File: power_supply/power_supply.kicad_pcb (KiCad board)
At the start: 2 copper layers, 150 x 70 mm, 55 parts, among them J1 Conn_01x04_Male, J2 Conn_01x03_Male, J3 Conn_01x03_Male, J4 Conn_01x03_Male, J5 Conn_01x02_Male, J6 Conn_01x02_Male, U1 LM7815_TO220, U2 LM7915_TO220, U3 LM7815_TO220

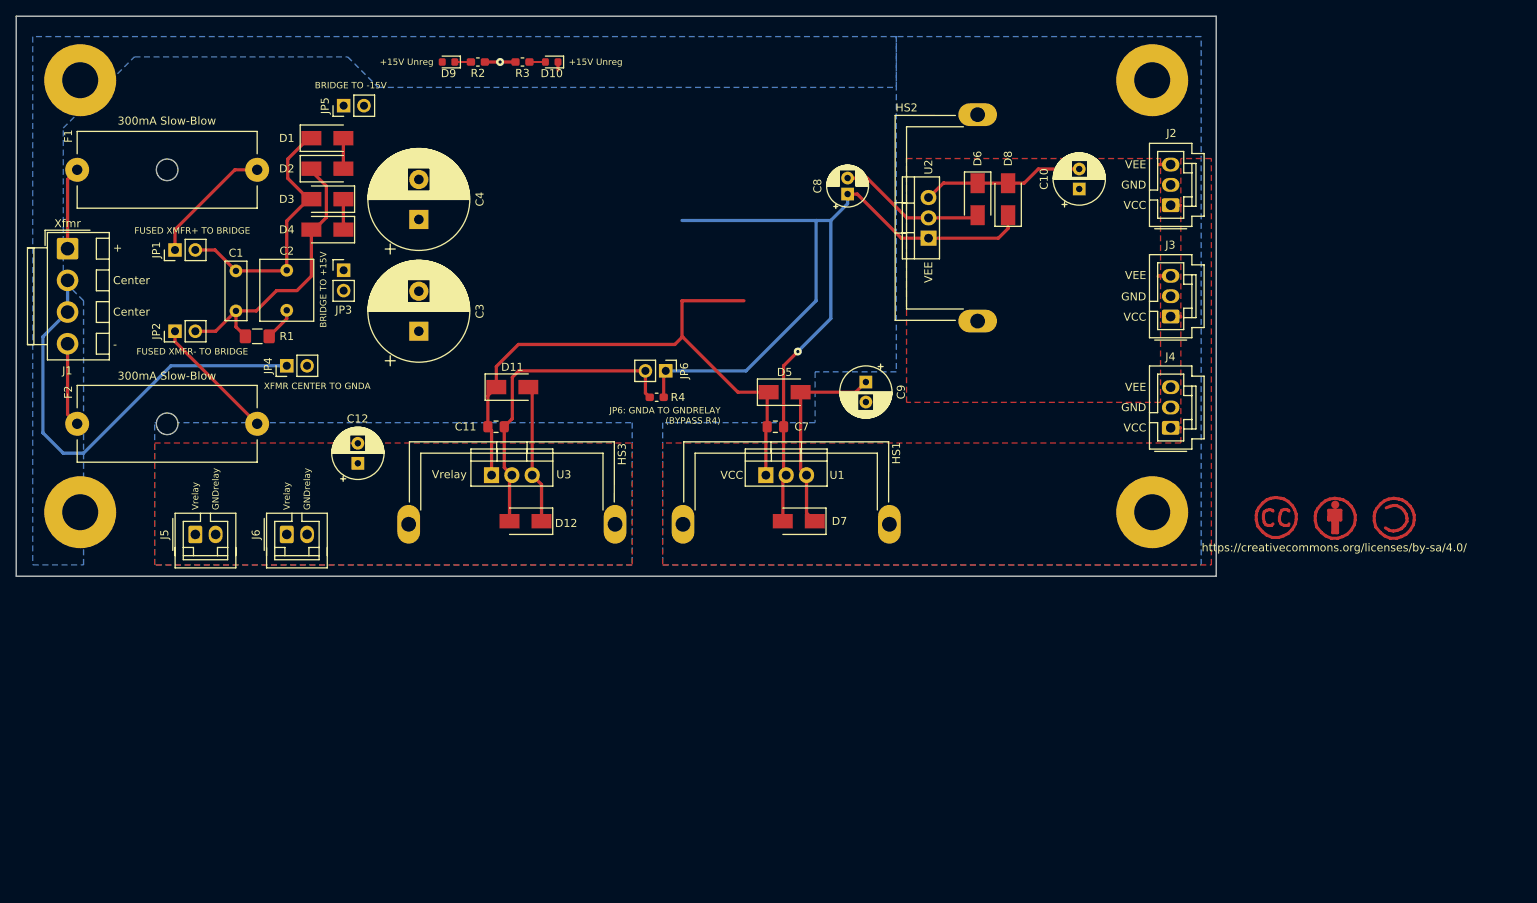
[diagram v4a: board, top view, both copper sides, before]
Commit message: correct silkscreen text for jumper JP6 based on schematic reannotation
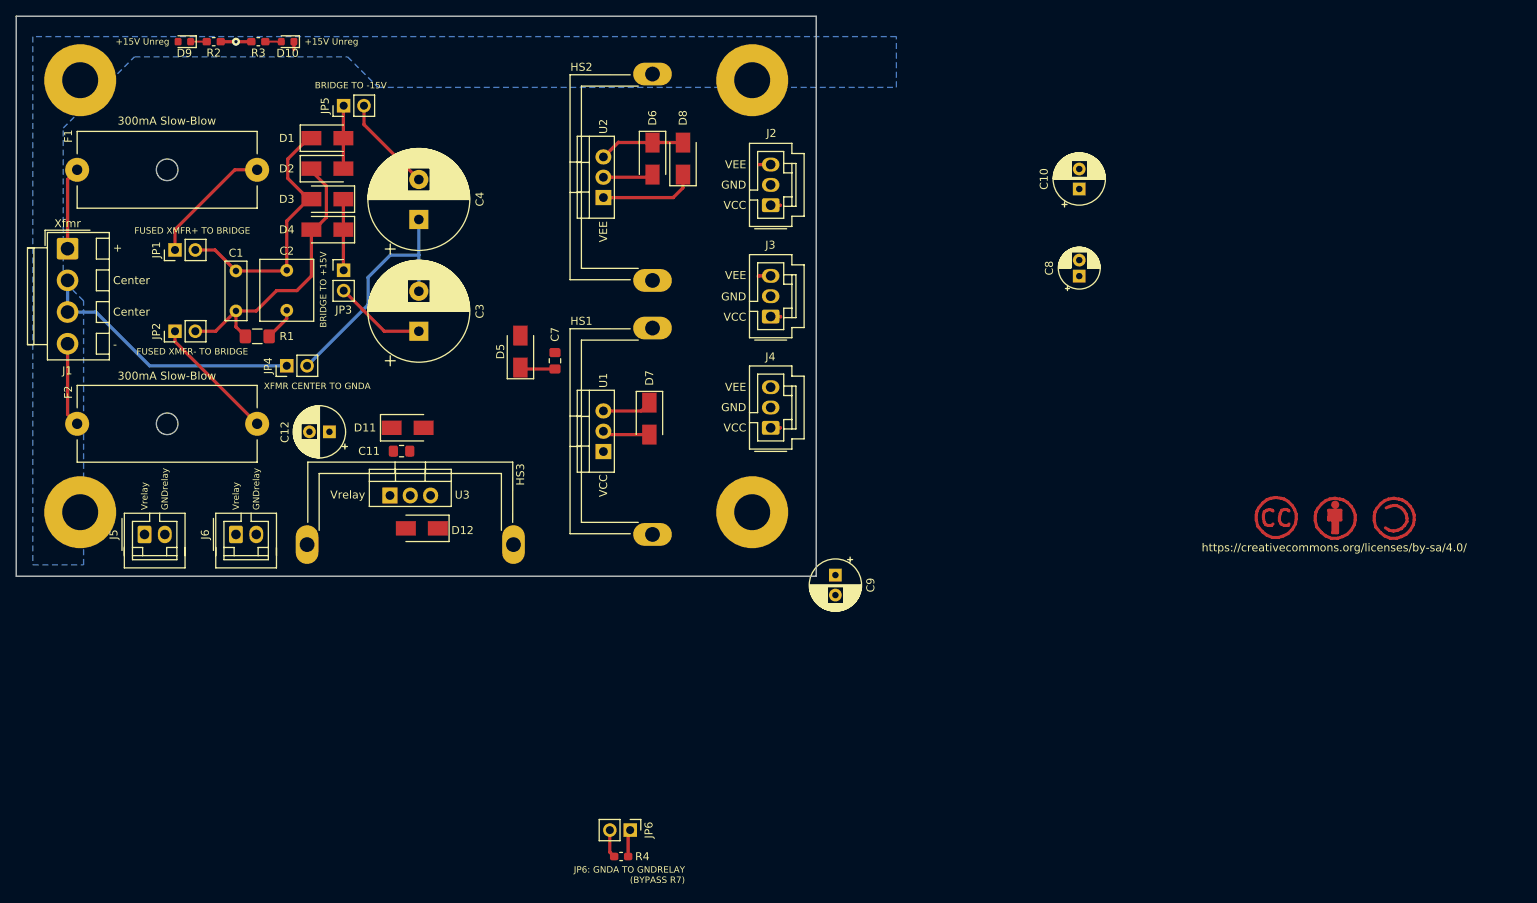
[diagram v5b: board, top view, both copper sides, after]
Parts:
- moved JP6 57.6 mm to (126.7, 181.7)
- moved R4 57.6 mm to (125.6, 185.0)
- moved H2 50.0 mm to (142.0, 88.0)
- moved H3 50.0 mm to (142.0, 142.0)
- moved J2 50.0 mm to (144.3, 103.6)
- moved J3 50.0 mm to (144.3, 117.5)
- moved J4 50.0 mm to (144.3, 131.5)
- moved D6 41.0 mm to (129.5, 97.8)
- moved D8 41.0 mm to (133.3, 97.8)
- moved HS2 41.0 mm to (129.5, 113.0)
- moved U2 41.0 mm to (123.4, 102.7)
- moved D5 33.4 mm to (113.0, 121.9), turned to 90 degrees
- moved D10 33.1 mm to (83.9, 83.2)
- moved R3 33.1 mm to (80.3, 83.2)
- moved D9 33.1 mm to (71.0, 83.2)
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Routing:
- net GNDA: track 128.5 -> 56.5 mm, vias 2 -> 1
- net /+15_unreg: track 75.8 -> 16.2 mm
- net GNDRELAY: track 39.4 -> 3.52 mm
- net /transformer_center: track 56.4 -> 34.1 mm
- net VCC: track 29.3 -> 9.90 mm
- net Vrelay: track 17.4 -> 0.00 mm
- net VEE: track 23.5 -> 13.8 mm
- net Net-(D3-Pad1): track 3.81 -> 8.90 mm
- net Net-(D1-Pad2): track 3.81 -> 7.89 mm
- removed copper zone on B.Cu, net GNDRELAY
- removed copper zone on F.Cu, net VCC
- removed copper zone on F.Cu, net VEE
- removed copper zone on F.Cu, net Vrelay
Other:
- board size 150 x 70 mm -> 100 x 70 mm
- board text added: "TODO fix C9, C10 add planes make smaller check to-220 dimensions for actual 7815 used add project rev, etc labels"
- board text removed: "TODO fix C9, C10 add planes make smaller check to-220 dimensions for actual 7815 used"

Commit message: finish basic routing. still need to thicken input traces, check TO-220 dims, and place labels/silkscreen decorations
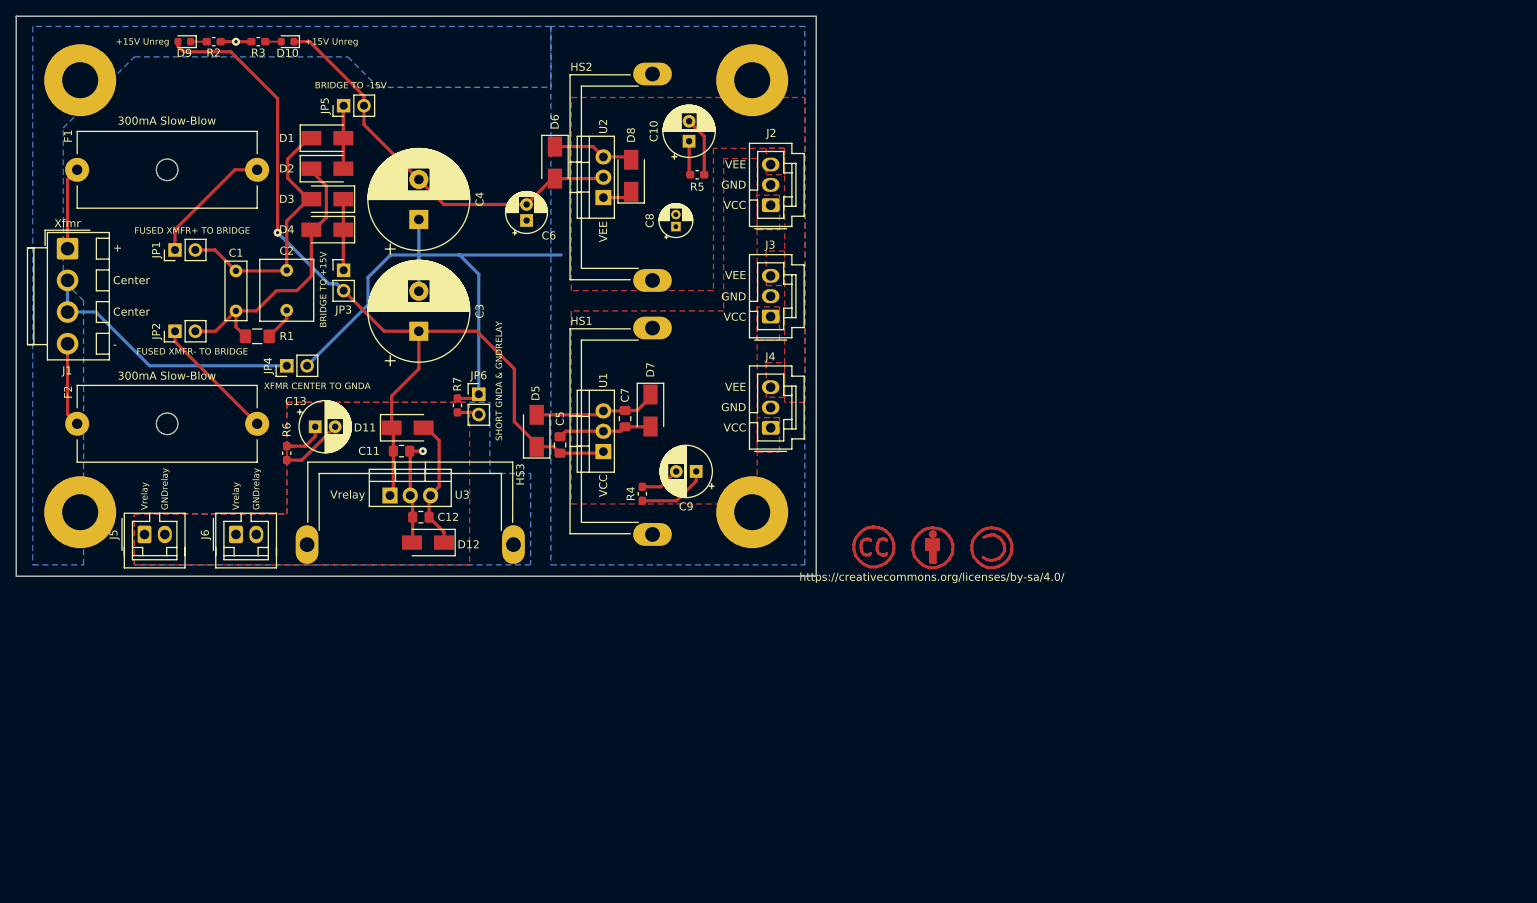
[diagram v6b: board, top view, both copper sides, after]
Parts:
- added C12: 100n, Capacitor_SMD:C_0805_2012Metric_Pad1.15x1.40mm_HandSolder, F.Cu at (100.6, 142.6)
- added C7: 100n, Capacitor_SMD:C_0805_2012Metric_Pad1.15x1.40mm_HandSolder, F.Cu at (126.1, 130.3)
- added C8: 1u, Capacitor_THT:CP_Radial_D4.0mm_P1.50mm, F.Cu at (132.5, 106.3)
- added R4: 100k, Capacitor_SMD:C_0603_1608Metric_Pad1.05x0.95mm_HandSolder, F.Cu at (128.3, 139.7)
- added R5: 100k, Capacitor_SMD:C_0603_1608Metric_Pad1.05x0.95mm_HandSolder, F.Cu at (135.1, 99.8)
- added R6: 100k, Capacitor_SMD:C_0603_1608Metric_Pad1.05x0.95mm_HandSolder, F.Cu at (83.8, 134.6)
- moved C6 69.4 mm to (113.8, 105.5)
- moved R7 60.0 mm to (105.2, 128.7), turned to 90 degrees
- moved JP6 57.7 mm to (107.8, 127.3), turned to 0 degrees
- moved REF** 50.4 mm to (157.1, 146.4)
- moved REF** 50.4 mm to (172.0, 146.4)
- moved REF** 50.4 mm to (164.6, 146.4)
- moved C10 49.1 mm to (134.1, 95.6)
- moved REF** 49.0 mm to (167.0, 119.9)
- moved REF** 47.5 mm to (175.0, 131.6)
- moved C9 21.7 mm to (135.0, 136.9), turned to 180 degrees
- moved D6 12.2 mm to (117.3, 98.3)
- moved C5 10.5 mm to (118.0, 133.6)
- moved D5 10.1 mm to (115.1, 131.8)
- moved D8 6.83 mm to (126.9, 99.9)
- moved D12 1.93 mm to (101.5, 145.8)
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- renumbered C12 to C13, C7 to C5, C8 to C6, R4 to R7
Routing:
- net /+15_unreg: track 16.2 -> 111.0 mm, vias 0 -> 1
- net GNDA: track 56.5 -> 99.0 mm
- net /-15_unreg: track 19.4 -> 50.7 mm
- net Vrelay: track 0.00 -> 21.9 mm
- net GNDRELAY: track 3.52 -> 23.8 mm, vias 0 -> 1
- net VCC: track 9.90 -> 24.4 mm
- net VEE: track 13.8 -> 17.7 mm
- added copper zone on B.Cu, net GNDRELAY
- added copper zone on F.Cu, net VCC
- added copper zone on F.Cu, net VEE
- added copper zone on F.Cu, net Vrelay
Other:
- net class grounds: clearance 0.4 -> 0.2
- board text added: "TODO add planes check to-220 dimensions for actual 7815 used add project rev, etc labels"
- board text removed: "TODO fix C9, C10 add planes make smaller check to-220 dimensions for actual 7815 used add project rev, etc labels"

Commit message: complete routing, including planes, thickening traces, and silkscreen labels
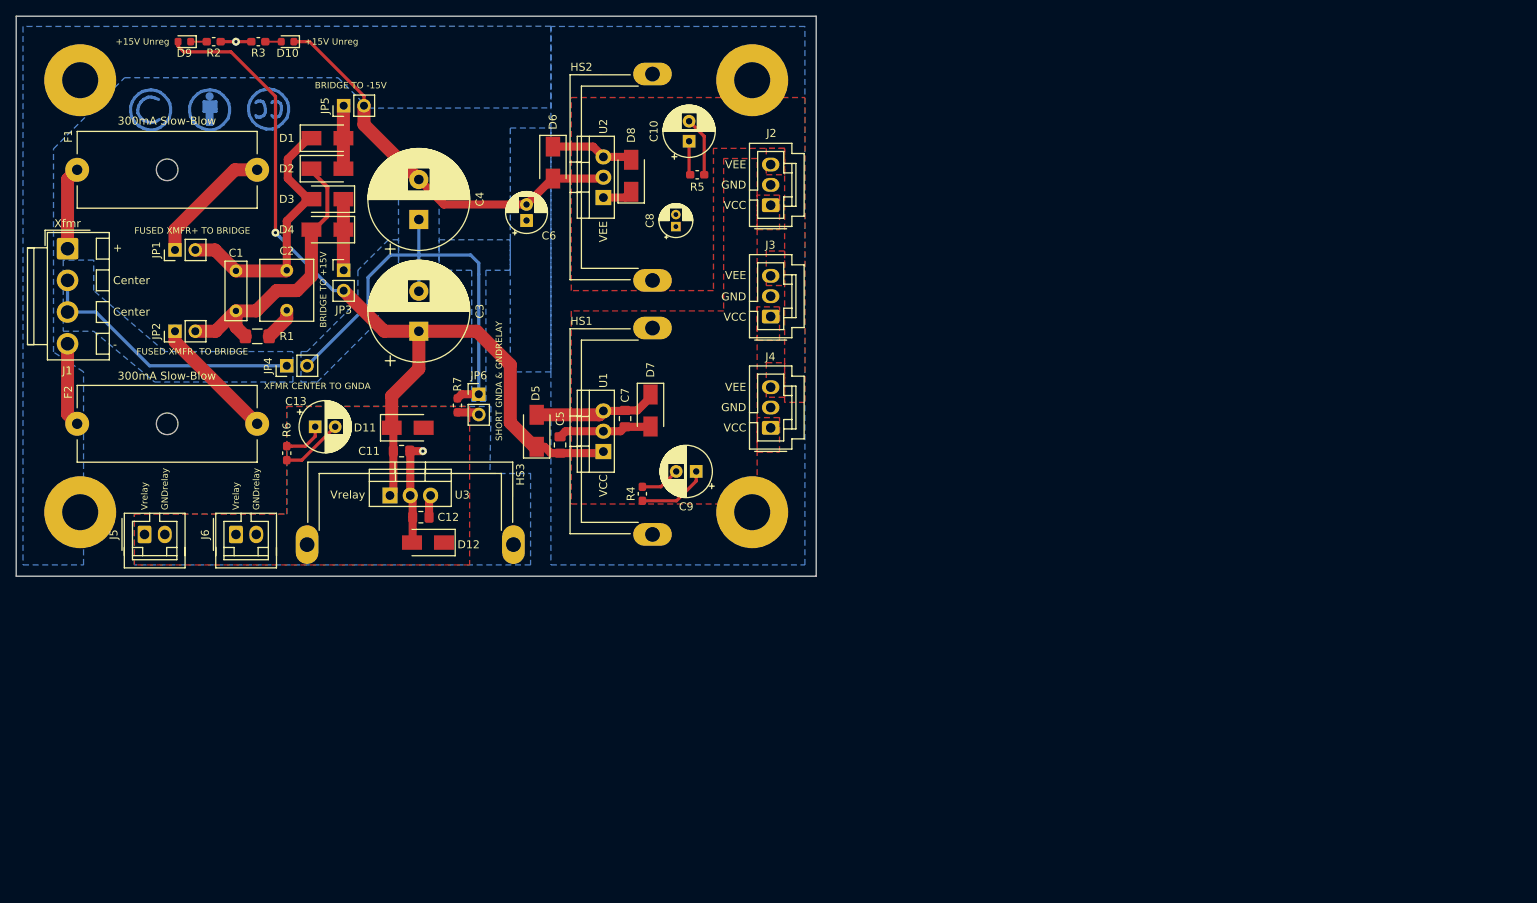
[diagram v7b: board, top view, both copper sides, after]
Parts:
- REF** (x3): moved to B.Cu
- moved REF** 118.5 mm to (66.8, 91.7), turned to 180 degrees
- moved REF** 105.7 mm to (74.2, 91.7), turned to 180 degrees
- moved REF** 93.1 mm to (81.7, 91.7), turned to 180 degrees
- moved REF** 73.4 mm to (110.5, 96.5)
- moved REF** 68.8 mm to (107.3, 85.6)
- moved D6 0.25 mm to (117.1, 98.3)
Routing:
- net Vrelay: track 21.9 -> 8.06 mm
- net GNDA: track 99.0 -> 87.1 mm
- added copper zone on B.Cu, net /transformer_center
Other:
- board text added: "Power Supply for Preamp 2019 rev0 G. Keeth"
- board text added: "TODO check to-220 dimensions for actual 7815 used"
- board text removed: "TODO add planes check to-220 dimensions for actual 7815 used add project rev, etc labels"

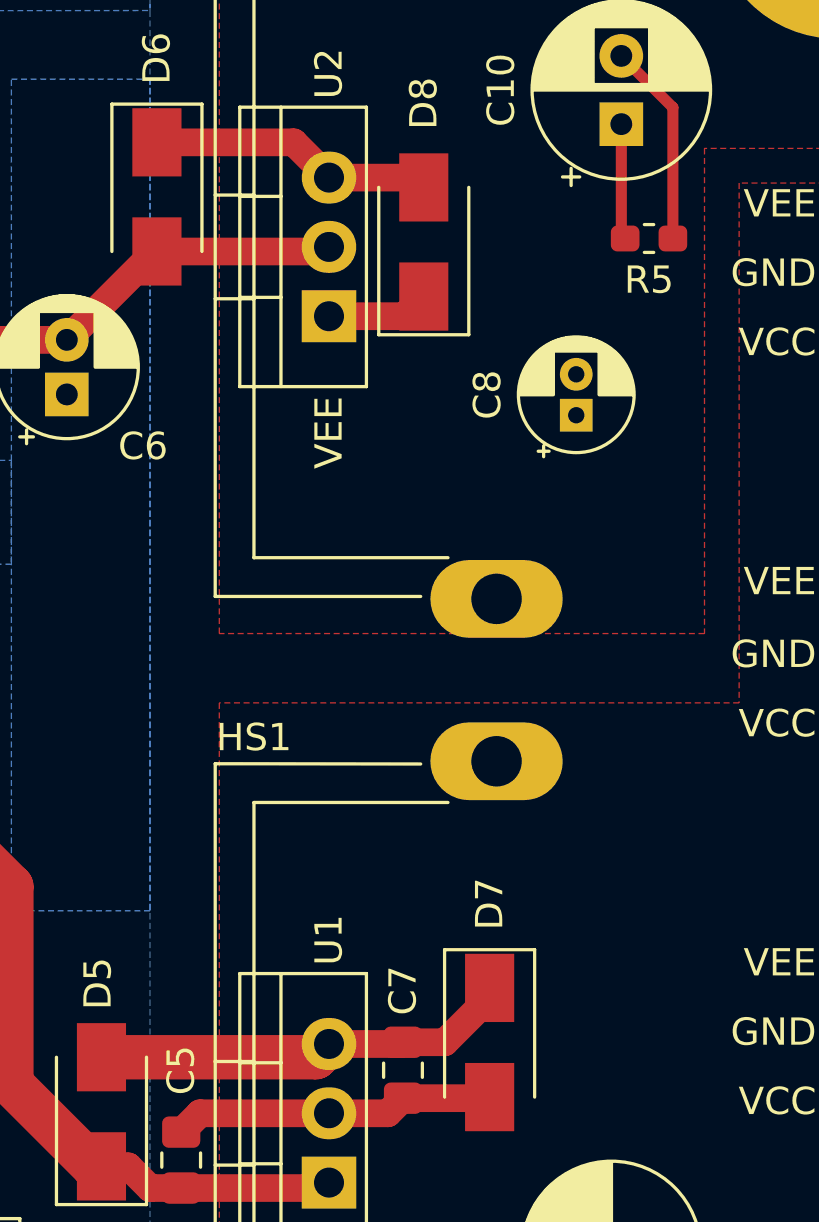
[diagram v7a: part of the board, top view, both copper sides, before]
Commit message: remove redundant traces
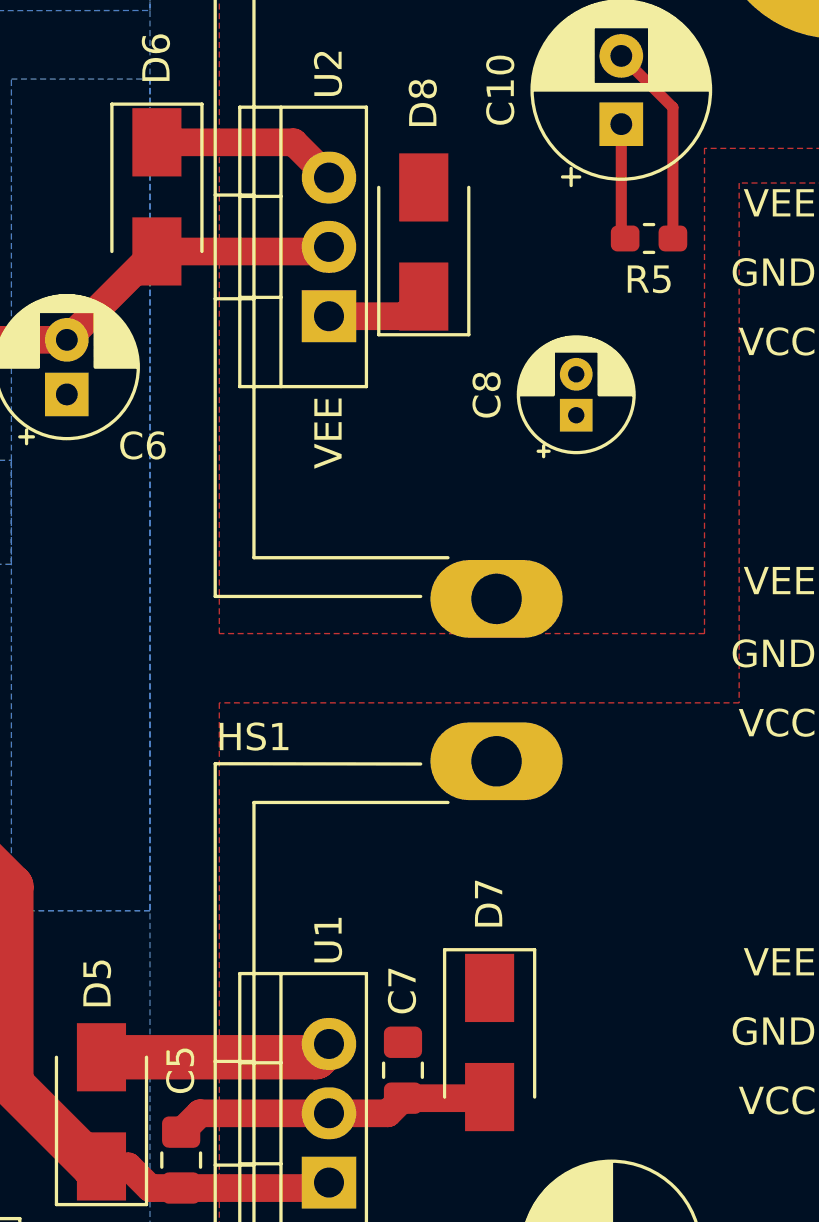
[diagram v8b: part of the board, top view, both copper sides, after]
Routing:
- net VCC: track 24.4 -> 17.5 mm
- net VEE: track 17.9 -> 14.3 mm
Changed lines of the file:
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@@
     (thickness 1.6)
     (drawings 10)
-    (tracks 153)
+    (tracks 146)
     (zones 0)
     (modules 61)
@@
   (segment (start 122.914 129.826) (end 123.4 129.34) (width 1.6256) (layer F.Cu) (net 4))
   (segment (start 115.062 129.826) (end 122.914 129.826) (width 1.6256) (layer F.Cu) (net 4))
-  (segment (start 126.048 129.34) (end 126.111 129.277) (width 1.016) (layer F.Cu) (net 4))
-  (segment (start 123.4 129.34) (end 126.048 129.34) (width 1.016) (layer F.Cu) (net 4))
-  (segment (start 129.286 127.636) (end 129.286 127.286) (width 1.016) (layer F.Cu) (net 4))
-  (segment (start 126.111 129.277) (end 127.645 129.277) (width 1.016) (layer F.Cu) (net 4))
-  (segment (start 127.645 129.277) (end 129.286 127.636) (width 1.016) (layer F.Cu) (net 4))
   (segment (start 135.001 138.1124) (end 135.001 136.906) (width 0.4064) (layer F.Cu) (net 4))
   (segment (start 132.5384 140.575) (end 135.001 138.1124) (width 0.4064) (layer F.Cu) (net 4))
   (segment (start 128.27 140.575) (end 132.5384 140.575) (width 0.4064) (layer F.Cu) (net 4))
-  (segment (start 126.514 97.59) (end 126.873 97.949) (width 1.016) (layer F.Cu) (net 5))
-  (segment (start 123.4 97.59) (end 126.514 97.59) (width 1.016) (layer F.Cu) (net 5))
   (segment (start 136.003 95.022) (end 136.003 99.822) (width 0.4064) (layer F.Cu) (net 5))
   (segment (start 134.112 93.131) (end 136.003 95.022) (width 0.4064) (layer F.Cu) (net 5))
-  (segment (start 122.108 96.298) (end 123.4 97.59) (width 1.016) (layer F.Cu) (net 5))
-  (segment (start 117.094 96.298) (end 122.108 96.298) (width 1.016) (layer F.Cu) (net 5))
+  (segment (start 122.108 96.298) (end 123.4 97.59) (width 1.016) (layer F.Cu) (net 5) (status 1000000))
+  (segment (start 117.094 96.298) (end 122.108 96.298) (width 1.016) (layer F.Cu) (net 5) (status 1000000))
   (segment (start 90.9 99.06) (end 90.9 95.25) (width 1.6256) (layer F.Cu) (net 6) (status 30))
   (segment (start 90.9 91.218) (end 90.932 91.186) (width 1.6256) (layer F.Cu) (net 6))
